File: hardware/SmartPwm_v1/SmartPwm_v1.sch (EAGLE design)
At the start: 37 parts, among them IC1 7805T, J1 ESP32-PICO-KIT, Q1 IRF3704-H, Q2 IRF3704-H, Q3 IRF3704-H, Q4 IRF3704-H, U1 ICL7667CPAZ, U2 ICL7667CPAZ

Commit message: swap out components for smt options, research jst 4 pin for leds
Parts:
- removed C2: .33uf, capacitor-wima:C2.5/2
- removed R1, R4, R5: 10K, rcl:R-US_0207/10
- removed R2: 10M, rcl:R-US_0207/10
- removed R3: 1M, rcl:R-US_0207/10
- removed U2: ICL7667CPAZ, ICL7667CPAZ:ICL7667CPAZ
- added C11: AVX_TPSA475K020R1800AVX_TPSA475K020R1800_0_0, AVX - TPSA475K020R1800:AVX_TPSA475K020R1800AVX_TPSA475K020R1800_0_0
- added C12: .1uf, rcl:C-USC0805
- added R10: 1M, rcl:R-US_R0805
- added R6, R8: 10K, rcl:R-US_R0805
- added R7: 10k, rcl:R-US_R0805
- added R9: 10M, rcl:R-US_R0805
- added U$8: TB002-500-P02, mylib:TB002-500-P02
- added U3: ICL7667CBAZA, ICL7667CBAZA:ICL7667CBAZA
- C1, C8: value .1uf -> 10uf; device capacitor-wima:C2.5/2 -> rcl:C-USC0805
- C10: value 10uf -> AVX_TPSA475K020R1800AVX_TPSA475K020R1800_0_0; device capacitor-wima:C2.5/2 -> AVX - TPSA475K020R1800:AVX_TPSA475K020R1800AVX_TPSA475K020R1800_0_0
- C3: value 4.7uf -> .33uf; device capacitor-wima:C2.5/2 -> rcl:C-USC0805
- C4, C5, C6, C9: device capacitor-wima:C2.5/2 -> rcl:C-USC0805
- C7: value 4.7uf -> .1uf; device capacitor-wima:C2.5/2 -> rcl:C-USC0805
- U$6: value 74AHTC125 -> 74AHTC125NSR; device DIP794W45P254L1969H508Q14:74AHTC125 -> DIP794W45P254L1969H508Q14:74AHTC125NSR
- U1: value ICL7667CPAZ -> ICL7667CBAZA; device ICL7667CPAZ:ICL7667CPAZ -> ICL7667CBAZA:ICL7667CBAZA
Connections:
- net CTRL1: now also U3.IN_A; no longer U1.IN_A
- net CTRL2: now also U3.IN_B; no longer U1.IN_B
- net CTRL3: now also U1.IN_A; no longer U2.IN_A
- net CTRL4: now also U1.IN_B; no longer U2.IN_B
- net GATE1: now also U3.OUT_A; no longer U1.OUT_A
- net GATE2: now also U3.OUT_B; no longer U1.OUT_B
- net GATE3: now also U1.OUT_A; no longer U2.OUT_A
- net GATE4: now also U1.OUT_B; no longer U2.OUT_B
- net GND: now also C10.CATHODE, C11.CATHODE, C12.2, R10.2, U$8.P$2, U3.V-; no longer C2.2, C8.2, R3.1, U2.V-
- net LOAD_RET1: now also C9.2; no longer C5.2
- net LOAD_RET3: now also C8.2; no longer C9.2
- net LOAD_RET4: now also C5.2; no longer C10.2
- net SCL: now also R7.2; no longer R4.2
- net SDA: now also R8.2; no longer R5.2
- net TDAT: now also R6.2; no longer R1.2
- net VCC: now also C4.1; no longer C1.1
- net VDD: now also C1.1, C10.ANODE, C11.ANODE, C12.1, R9.1, U$8.P$1, U3.V+; no longer C10.1, C2.1, C4.1, R2.2, U2.V+
- net VDIV: now also R10.1, R9.2; no longer R2.1, R3.2
- net VEE: now also R6.1, R7.1, R8.1; no longer R1.1, R4.1, R5.1
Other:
- moved on the sheet: C1, C3, C4, C5, C7, C8, C9, U1

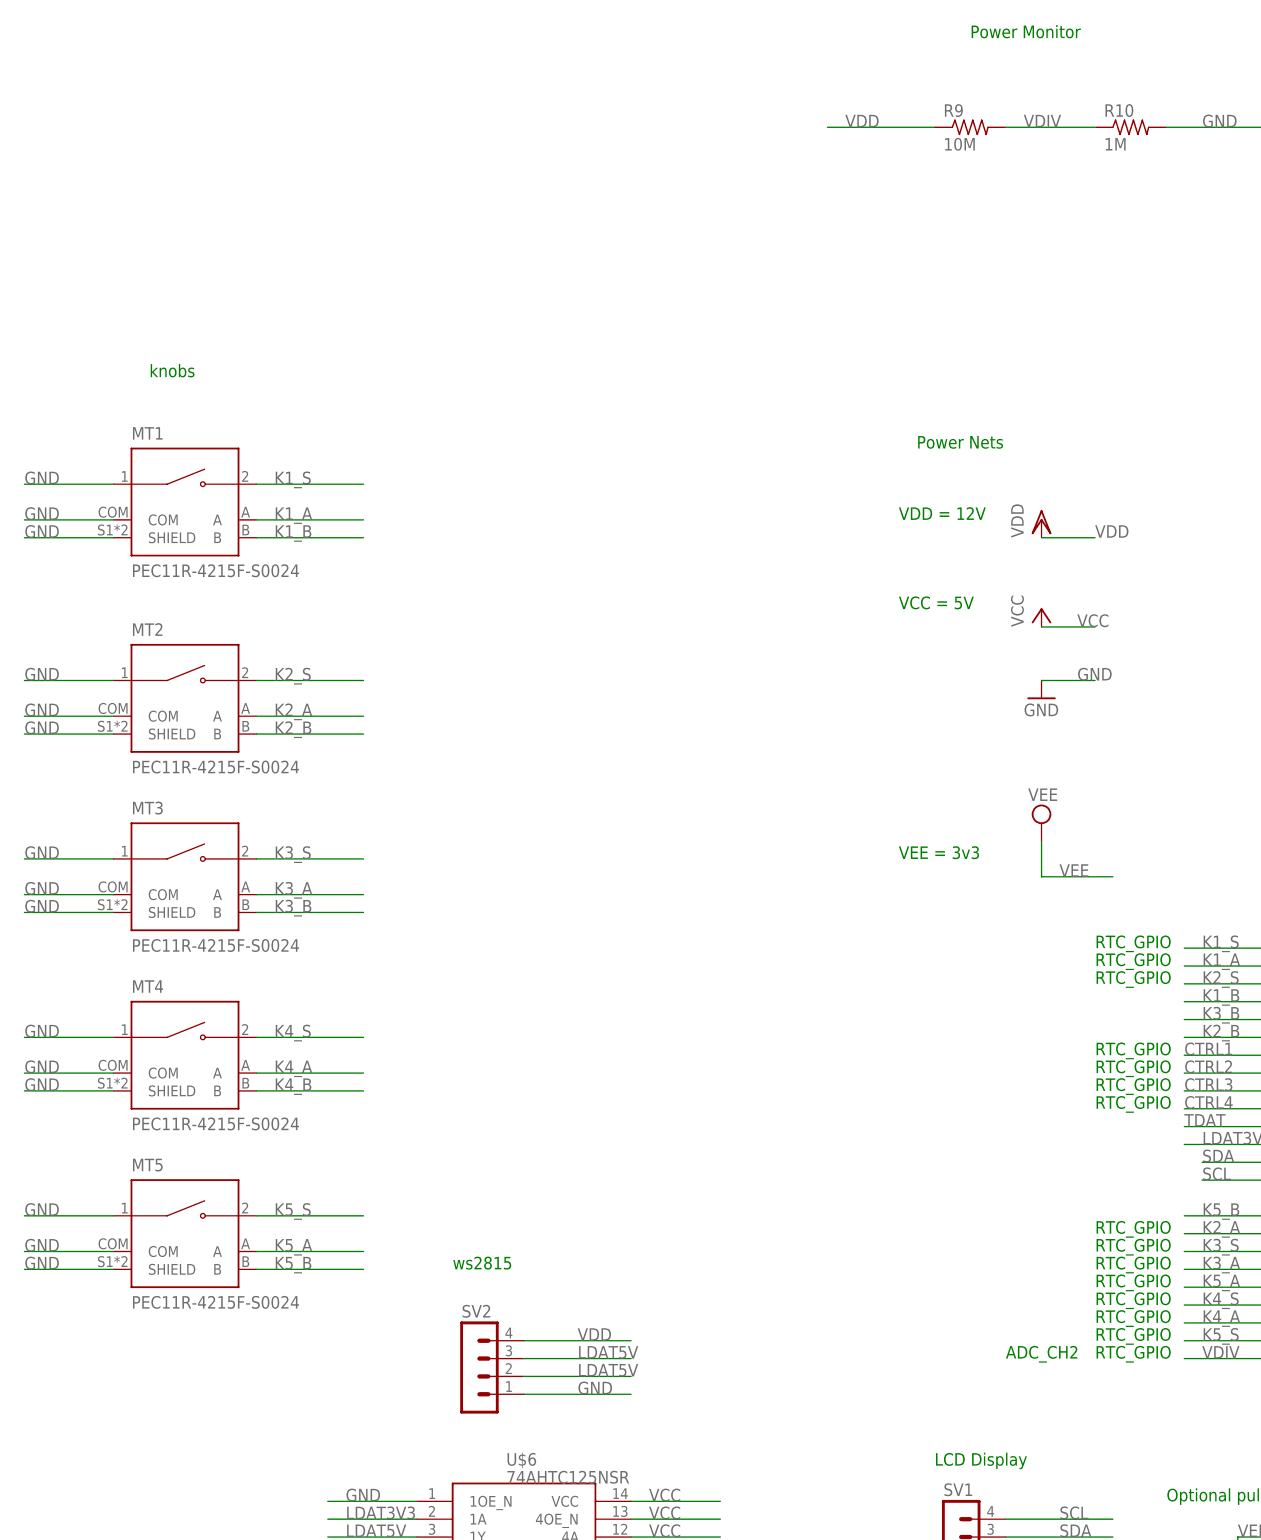
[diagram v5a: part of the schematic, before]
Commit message: add 3 more led strips, time to start layout!
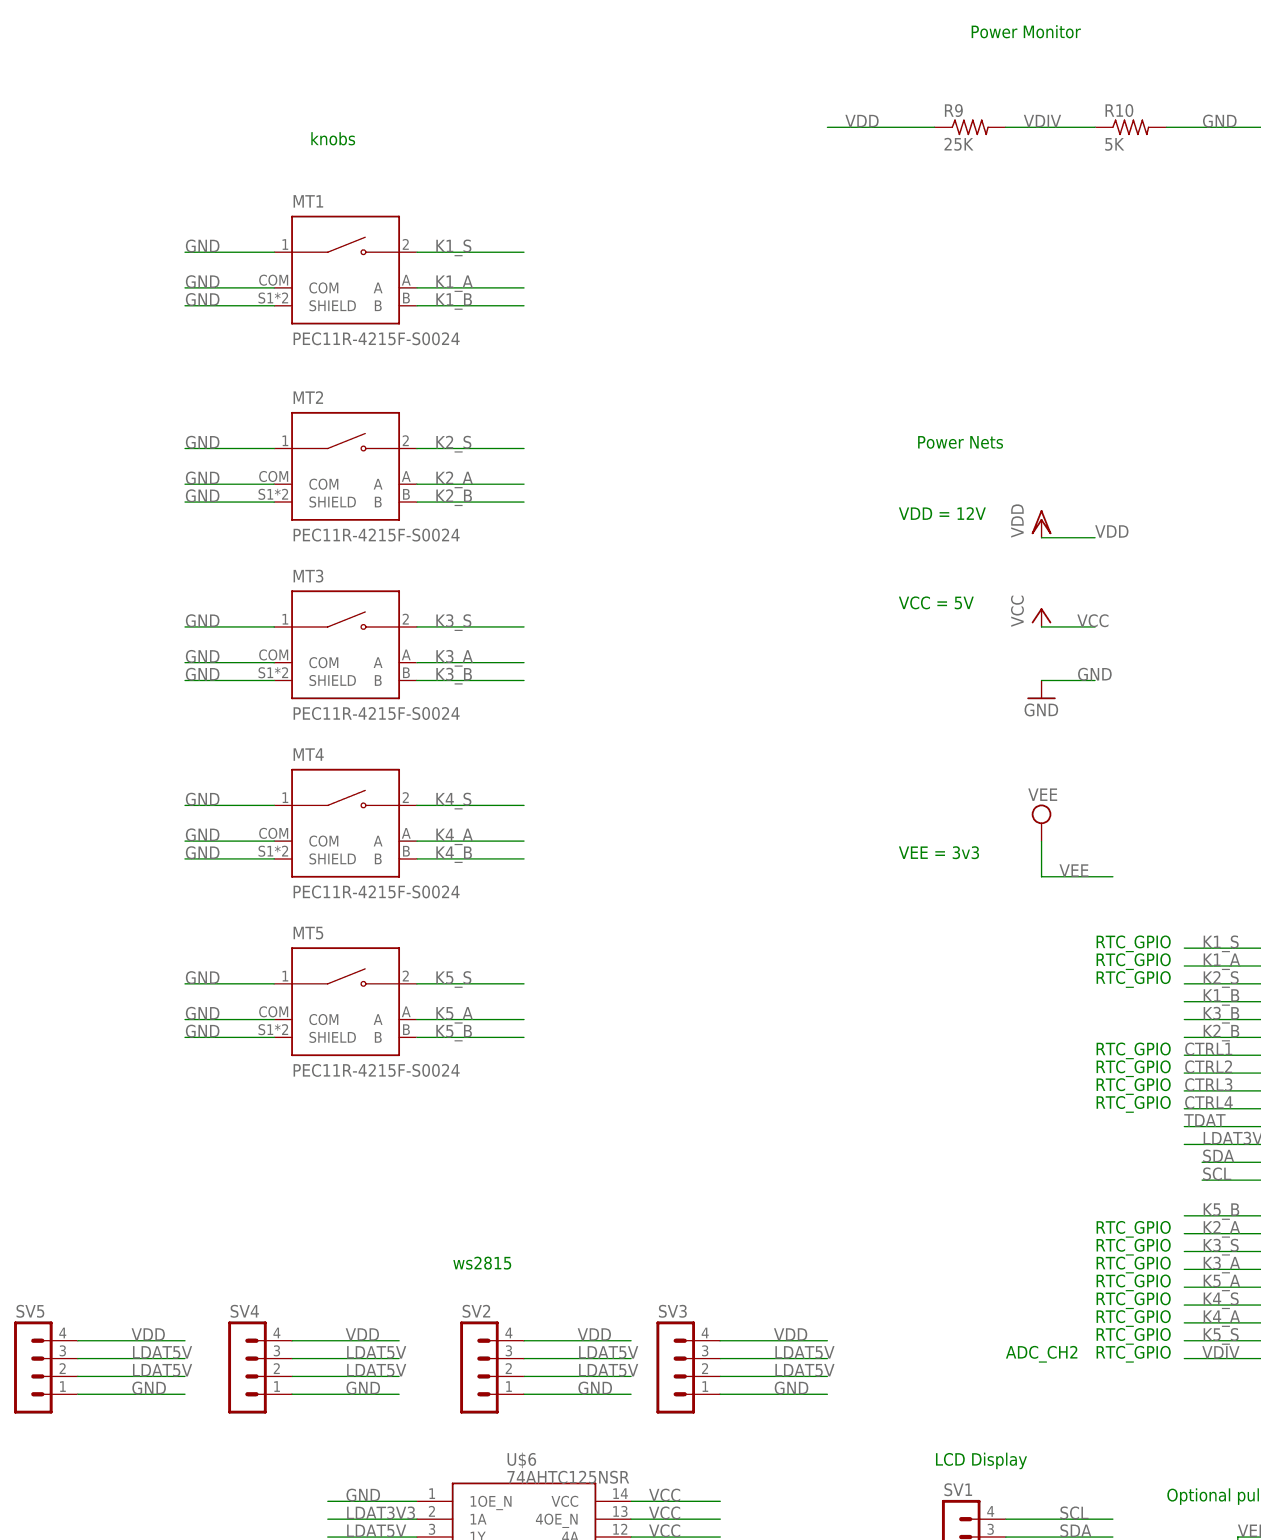
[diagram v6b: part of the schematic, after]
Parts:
- added SV3, SV4, SV5: (no value), con-lstb:MA04-1
- R10: value 1M -> 5K
- R9: value 10M -> 25K
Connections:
- net GND: now also SV3.1, SV4.1, SV5.1
- net LDAT5V: now also SV3.2, SV3.3, SV4.2, SV4.3, SV5.2, SV5.3
- net VDD: now also SV3.4, SV4.4, SV5.4
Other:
- moved on the sheet: MT1, MT2, MT3, MT4, MT5

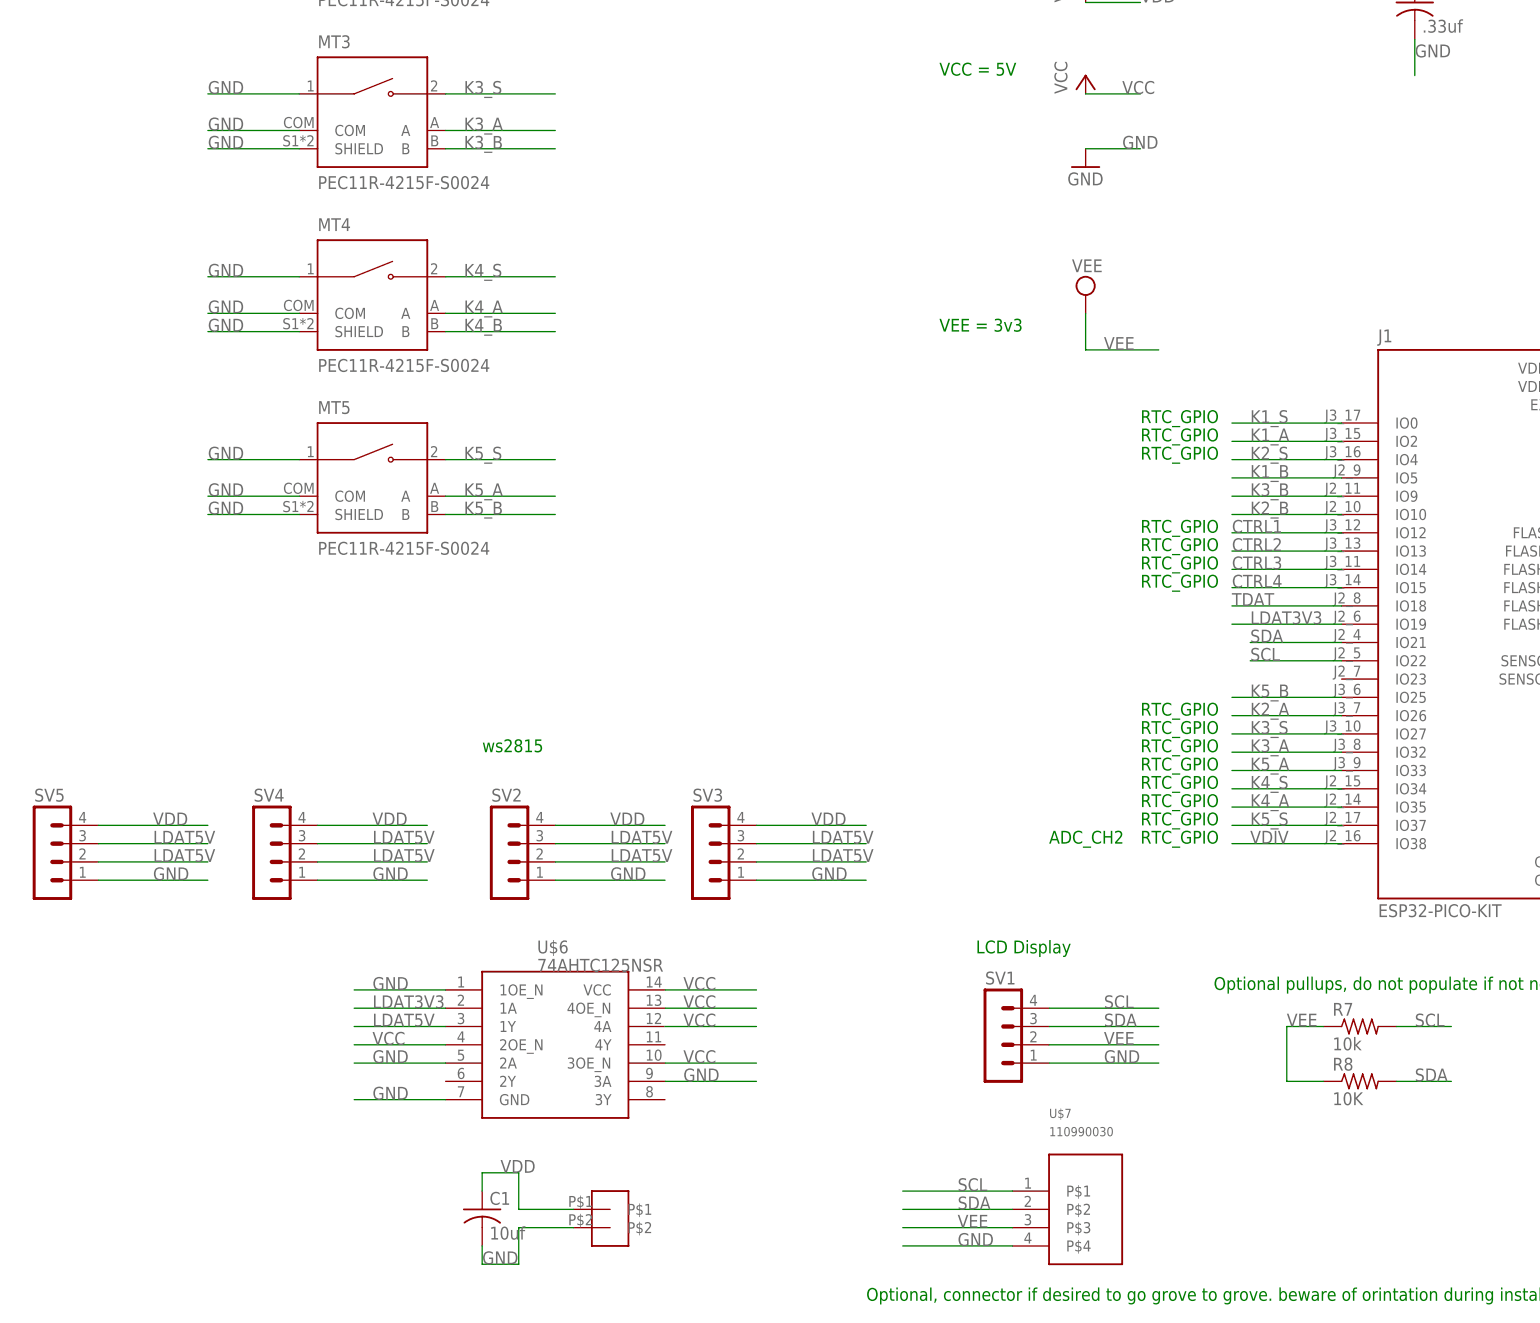
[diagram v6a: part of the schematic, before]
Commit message: remove 1 knob, add 3 individual leds, start component placment
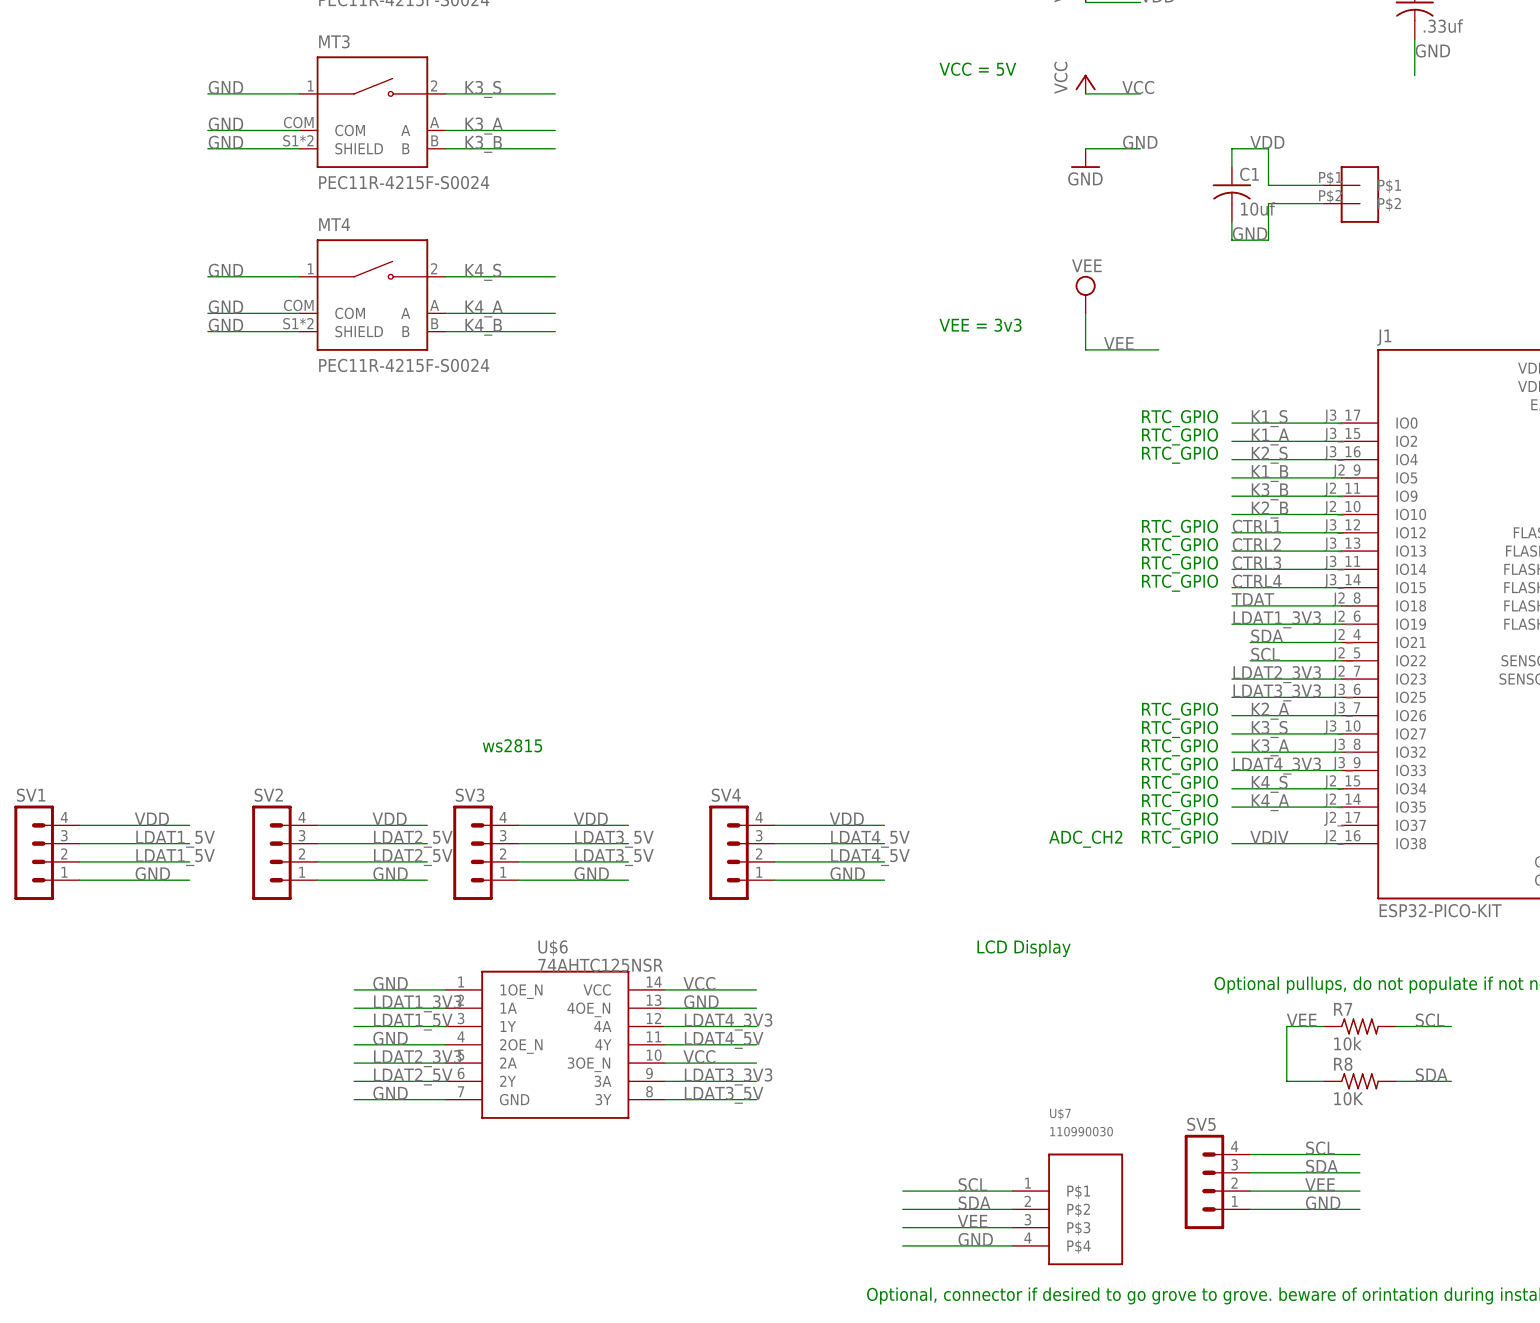
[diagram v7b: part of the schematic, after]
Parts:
- removed MT5: PEC11R-4215F-S0024, PEC11R-4215F-S0024:PEC11R-4215F-S0024
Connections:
- net LDAT3V3 renamed LDAT1_3V3
- removed net K5_A: J1.IO33, MT5.A
- removed net K5_B: J1.IO25, MT5.B
- removed net K5_S: J1.IO37, MT5.2
- removed net LDAT5V: SV2.2, SV2.3, SV3.2, SV3.3, SV4.2, SV4.3, SV5.2, SV5.3, U$6.1Y
- new net LDAT1_5V: SV1.2, SV1.3, U$6.1Y
- new net LDAT2_3V3: J1.IO23, U$6.2A
- new net LDAT2_5V: SV2.2, SV2.3, U$6.2Y
- new net LDAT3_3V3: J1.IO25, U$6.3A
- new net LDAT3_5V: SV3.2, SV3.3, U$6.3Y
- new net LDAT4_3V3: J1.IO33, U$6.4A
- new net LDAT4_5V: SV4.2, SV4.3, U$6.4Y
- net GND: now also U$6.2OE_N, U$6.4OE_N; no longer MT5.1, MT5.COM, MT5.SHIELD, U$6.2A, U$6.3A
- net SCL: now also SV5.4; no longer SV1.4
- net SDA: now also SV5.3; no longer SV1.3
- net VCC: no longer U$6.2OE_N, U$6.4A, U$6.4OE_N
- net VDD: now also SV1.4; no longer SV5.4
- net VEE: now also SV5.2; no longer SV1.2
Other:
- moved on the sheet: C1, SV1, SV2, SV3, SV4, SV5
